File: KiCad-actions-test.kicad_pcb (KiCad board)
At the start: 2 copper layers, 57.2 x 36.8 mm, 3 parts

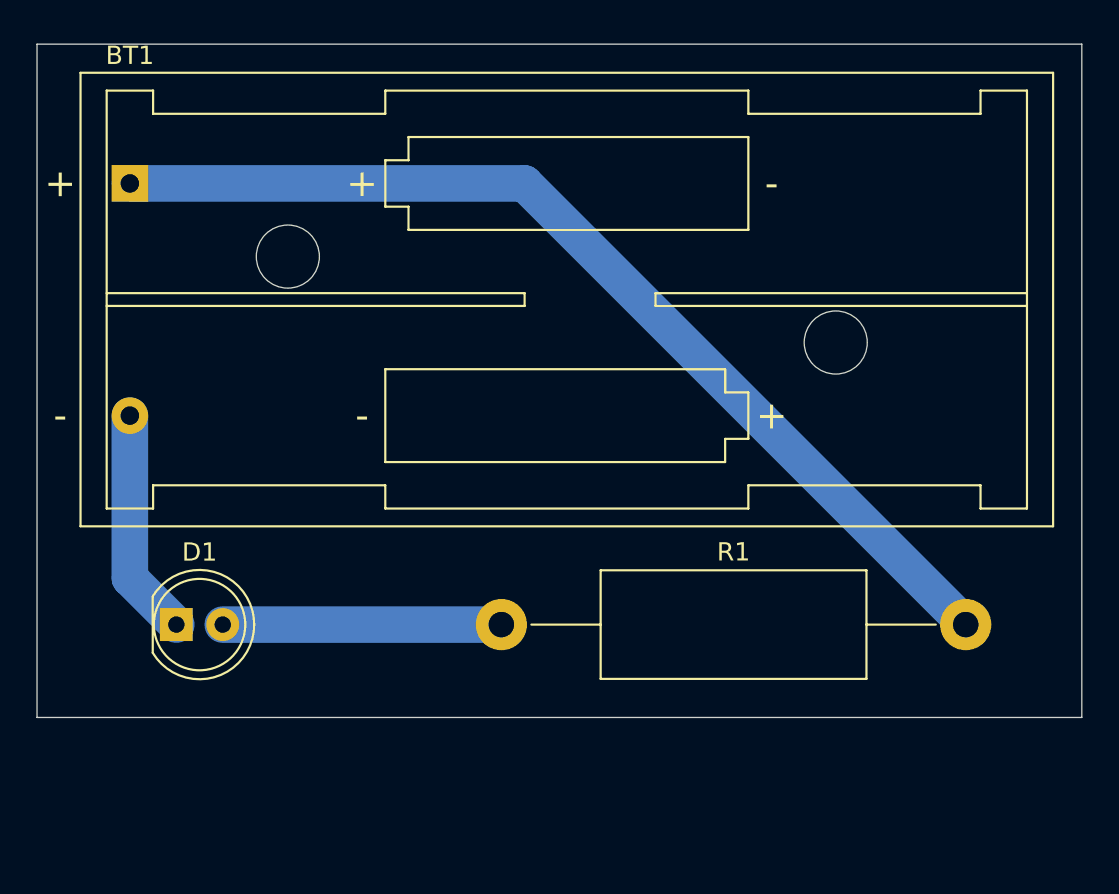
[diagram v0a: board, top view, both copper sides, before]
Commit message: add one more led
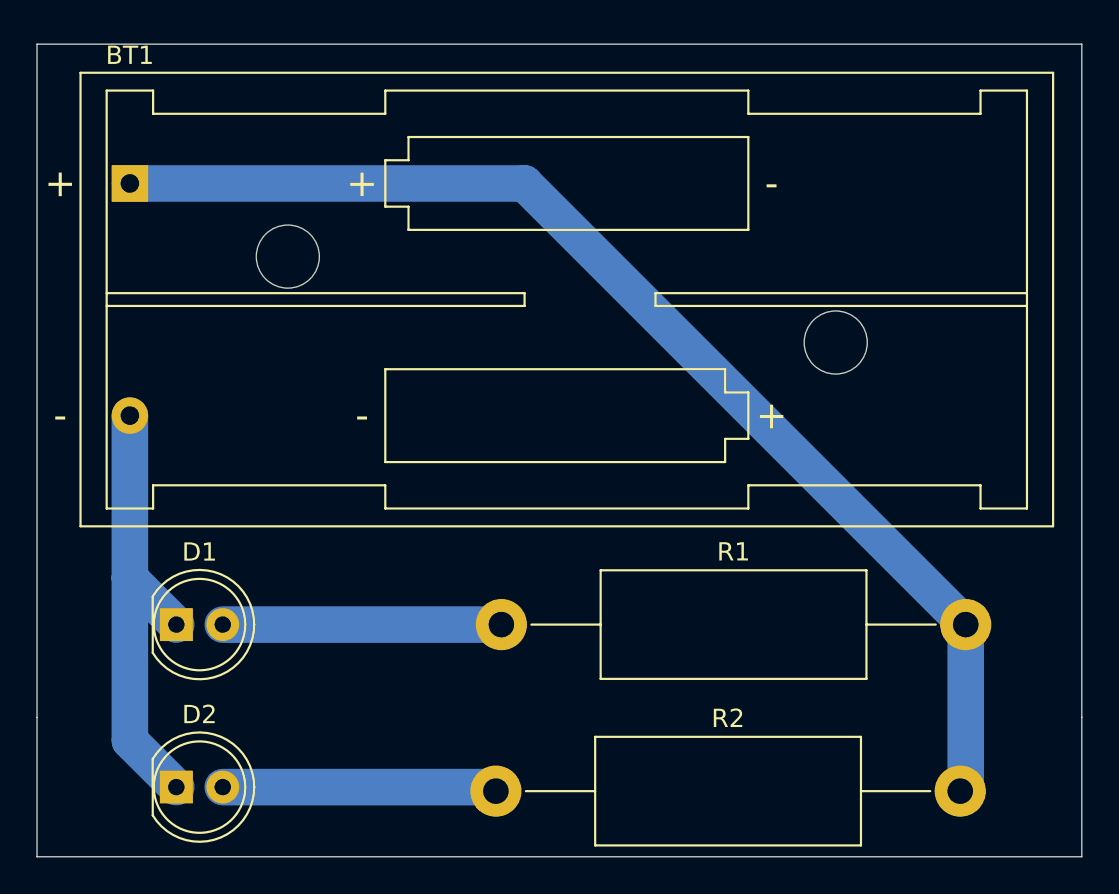
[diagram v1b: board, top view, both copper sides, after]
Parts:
- added D2: red LED, LED_THT:LED_D5.0mm, F.Cu at (109.2, 135.9)
- added R2: 330, Resistor_THT:R_Axial_DIN0614_L14.3mm_D5.7mm_P25.40mm_Horizontal, F.Cu at (126.7, 136.1)
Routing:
- net Net-(D2-Pad2): track 0.00 -> 15.0 mm
- net GND: track 12.5 -> 25.0 mm
- net Net-(BT1-Pad1): track 55.7 -> 64.9 mm
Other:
- board size 57.2 x 36.8 mm -> 57.2 x 44.4 mm
